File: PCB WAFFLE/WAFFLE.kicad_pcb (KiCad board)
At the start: 2 copper layers, 61 x 48 mm, 24 parts, among them IC1 STM32L412KBT6, J2 FTSH-107-01-L-DV, J7 Conn_01x03_Male

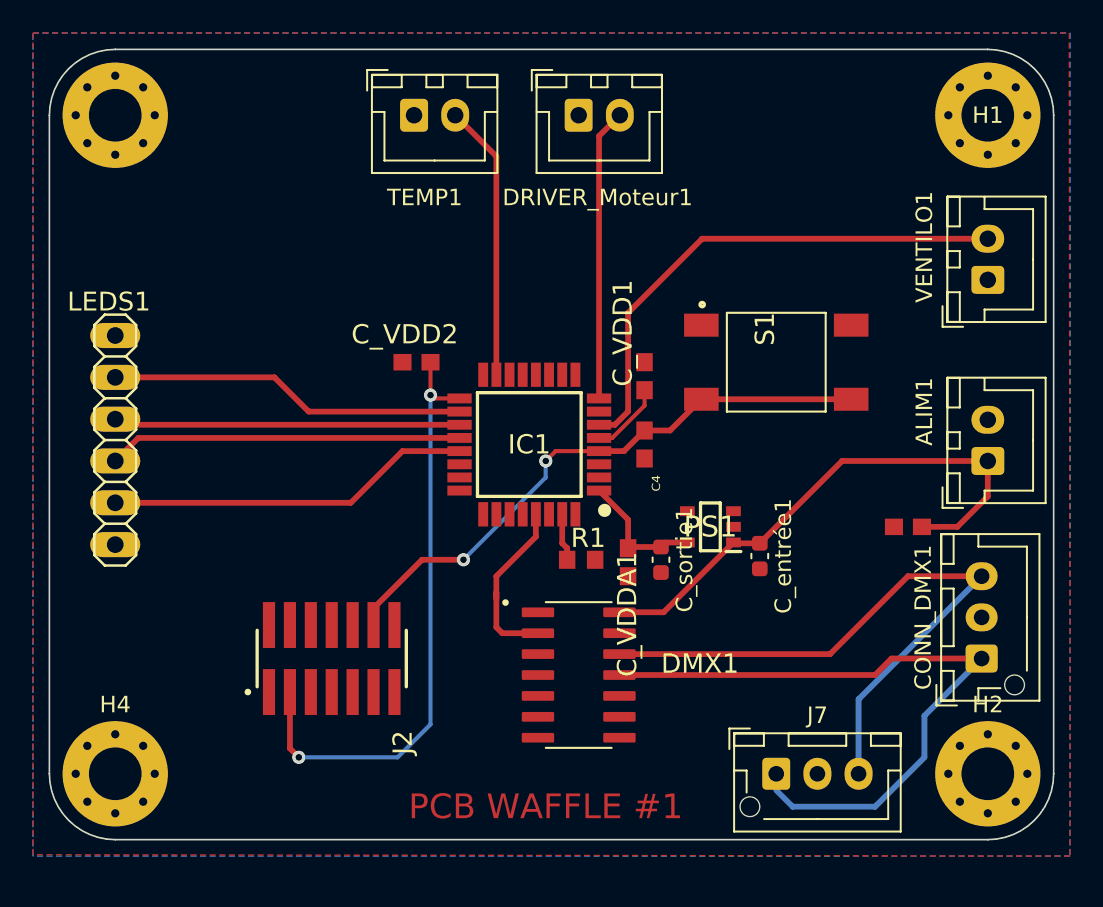
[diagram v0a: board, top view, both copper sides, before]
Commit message: Add files via upload
Version du 28/02 du pcb de contrôle (ajout d'un système de driver pour le ventilo)
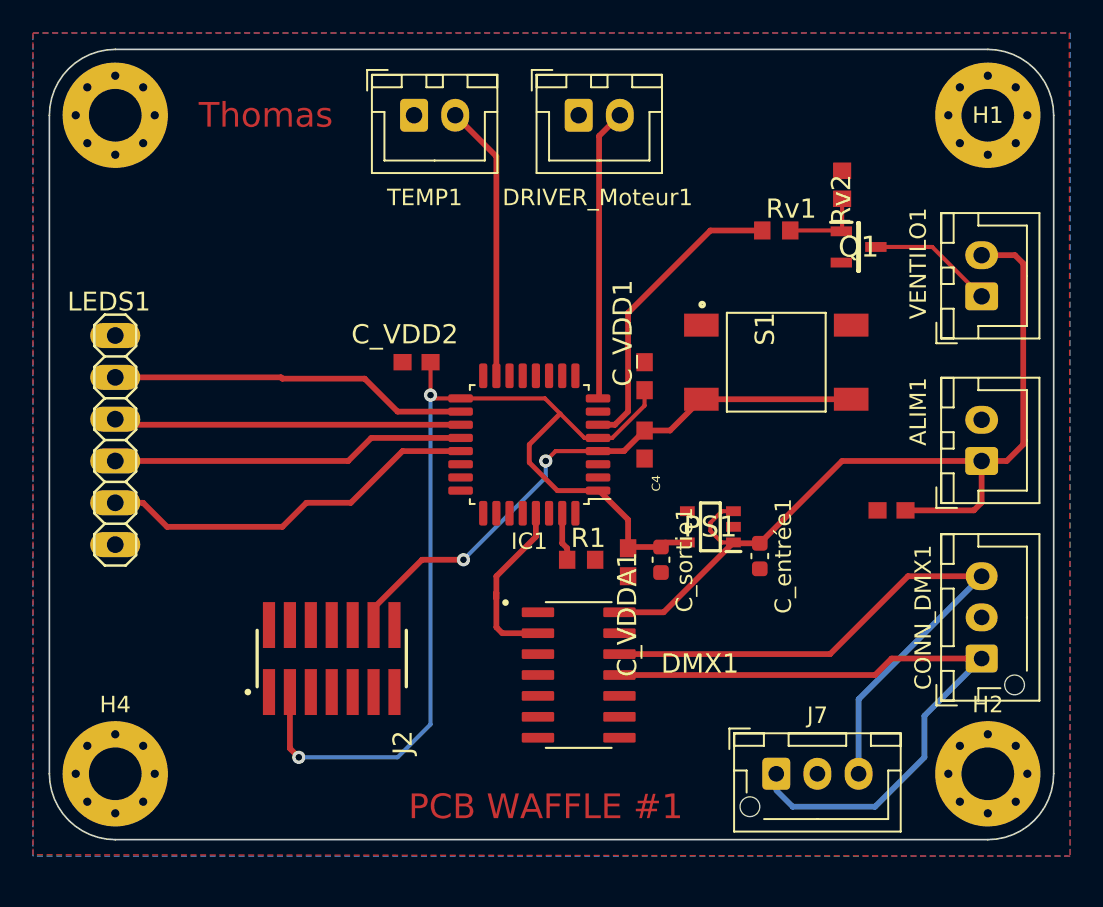
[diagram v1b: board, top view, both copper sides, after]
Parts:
- added Q1: SQ2310ES-T1_GE3, stm32l021:SOT95P237X112-3N, F.Cu at (191.0, 82.0)
- added Rv1: 22, stm32l021:R0603, F.Cu at (186.0, 81.0)
- added Rv2: 10k, stm32l021:R0603, F.Cu at (190.0, 78.2)
- C_sortie1: value 1uF -> 4.7uF
- DMX1: value >VALUE -> SOIC127P600X175-14N
- IC1: footprint stm32l021:QFP80P900X900X160-32N -> Package_QFP:LQFP-32_7x7mm_P0.8mm
- moved C_Decoupl_Connecteur1 1.41 mm to (193.0, 98.0)
- moved VENTILO1 1.07 mm to (198.5, 85.0)
- moved ALIM1 0.38 mm to (198.5, 95.0)
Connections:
- CONN_DMX1 pad 1: Net-(DMX1-Pad11) -> Net-(CONN_DMX1-Pad1)
- CONN_DMX1 pad 3: Net-(DMX1-Pad12) -> Net-(CONN_DMX1-Pad3)
- C_Decoupl_Connecteur1 pad 1: unconnected-(C_Decoupl_Connecteur1-Pad1) -> GND
- DMX1 pad 11: Net-(DMX1-Pad11) -> Net-(CONN_DMX1-Pad1)
- DMX1 pad 12: Net-(DMX1-Pad12) -> Net-(CONN_DMX1-Pad3)
- IC1 pad 29: unconnected-(DMX1-Pad2) -> UART_RS485_DMX
- J7 pad 1: Net-(DMX1-Pad11) -> unconnected-(J7-Pad1)
- J7 pad 3: Net-(DMX1-Pad12) -> unconnected-(J7-Pad3)
- LEDS1 pad 6: GND -> unconnected-(LEDS1-Pad6)
- PS1 pad 2: Net-(PS1-Pad2) -> GND
- PS1 pad 3: Net-(PS1-Pad2) -> +5V
- VENTILO1 pad 1: GND -> Net-(VENTILO1-Pad1)
- VENTILO1 pad 2: PWM_Ventilateur -> +5V
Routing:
- net Net-(DMX1-Pad11): track 41.5 -> 0.00 mm
- net Net-(CONN_DMX1-Pad1): track 0.00 -> 41.5 mm
- net Net-(DMX1-Pad12): track 39.1 -> 0.00 mm
- net Net-(CONN_DMX1-Pad3): track 0.00 -> 39.1 mm
- net +5V: track 33.1 -> 53.7 mm
- net +3.3V: track 49.3 -> 67.5 mm
- net PWM_Ventilateur: track 32.5 -> 18.3 mm
- net unconnected-(DMX1-Pad2): track 10.9 -> 0.00 mm
- net UART_RS485_DMX: track 0.00 -> 10.9 mm
- net Net-(VENTILO1-Pad1): track 0.00 -> 7.67 mm
- net Net-(Rv1-Pad2): track 0.00 -> 5.15 mm
- net PWM_Leds_R: track 22.2 -> 23.4 mm
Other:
- board text added: "Thomas"

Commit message: Add files via upload
Après remarques du professeur : Erreurs de routage (CRC) corrigées, changement de l'empreinte du connecteur LED par un jst (et correction des empreintes connecteurs DMX), connexion de l'uart pour la sonde (oubli).
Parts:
- CONN_DMX1, J7: footprint Connector_JST:JST_XH_B3B-XH-AM_1x03_P2.50mm_Vertical -> Connector_JST:JST_XH_B3B-XH-A_1x03_P2.50mm_Vertical
- LEDS1: footprint stm32l021:1X06 -> Connector_JST:JST_XH_B6B-XH-A_1x06_P2.50mm_Vertical
- moved DRIVER_Moteur1 43.5 mm to (157.0, 114.0)
- moved J2 34.9 mm to (175.0, 76.0), turned to -90 degrees
- moved LEDS1 5.84 mm to (147.0, 88.0)
- moved H1 0.15 mm to (199.0, 74.0)
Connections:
- DMX1 pad 2: unconnected-(DMX1-Pad2) -> UART_RS485_DMX
- IC1 pad 29: UART_RS485_DMX -> UART_Driver_moteur
- IC1 pad 30: unconnected-(IC1-Pad30) -> UART_RS485_DMX
- IC1 pad 8: UART_Driver_moteur -> VCP_UART_TX
- IC1 pad 9: unconnected-(IC1-Pad9) -> VCP_UART_RX
- J7 pad 1: unconnected-(J7-Pad1) -> Net-(CONN_DMX1-Pad1)
- J7 pad 3: unconnected-(J7-Pad3) -> Net-(CONN_DMX1-Pad3)
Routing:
- net Net-(CONN_DMX1-Pad1): track 41.5 -> 29.2 mm
- net VCP_UART_TX: track 0.00 -> 12.2 mm
- net +3.3V: track 67.5 -> 56.5 mm
- net VCP_UART_RX: track 0.00 -> 10.5 mm
- net UART_Driver_moteur: track 17.7 -> 21.9 mm
- net PWM_Leds_R: track 23.4 -> 21.3 mm
- net UART_RS485_DMX: track 10.9 -> 9.08 mm
- net PWM_Leds_W: track 21.8 -> 20.4 mm
- net PWM_Leds_B: track 21.1 -> 19.9 mm
- net PWM_Leds_G: track 21.6 -> 20.6 mm
- net NRST: track 35.9 -> 36.7 mm
- net Net-(CONN_DMX1-Pad3): track 39.1 -> 39.4 mm, vias 0 -> 2
